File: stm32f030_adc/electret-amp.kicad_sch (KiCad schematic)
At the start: 11 parts, among them Q1 BC337

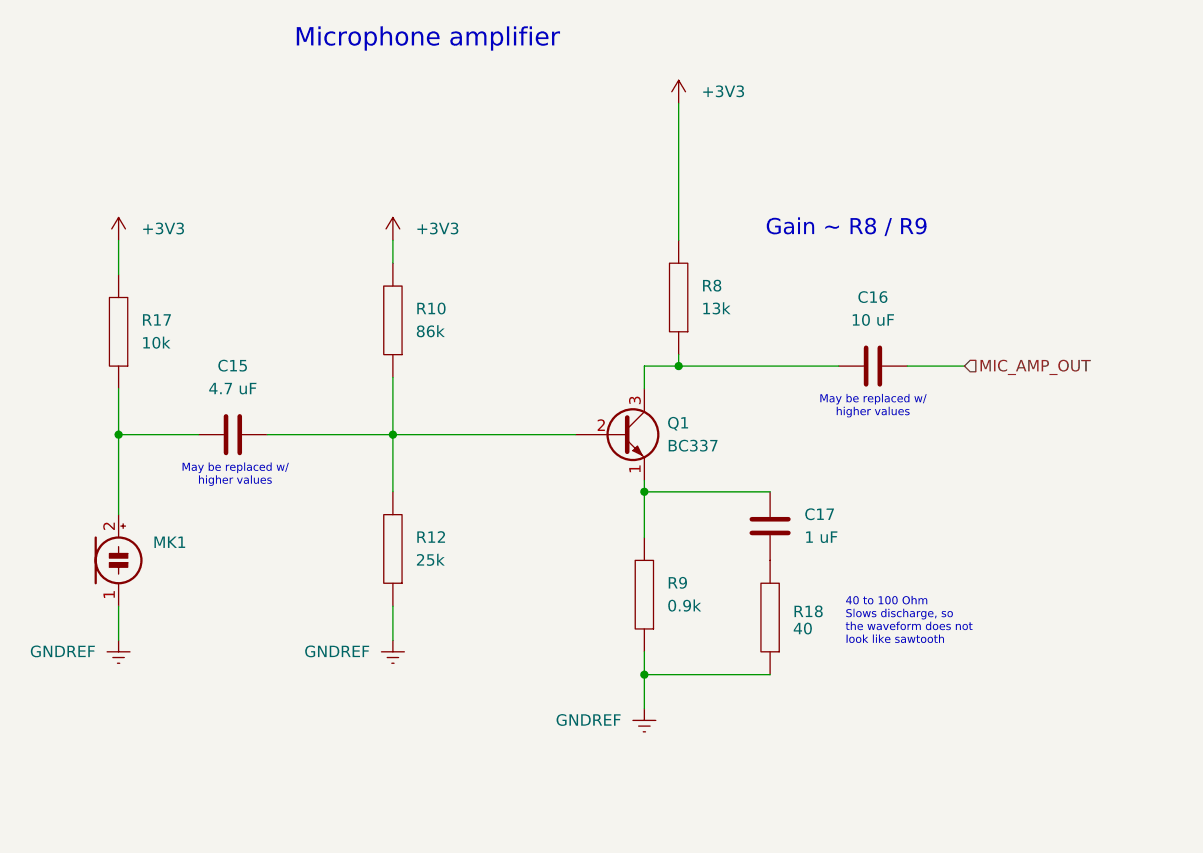
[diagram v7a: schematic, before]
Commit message: [schematics] Impl |  Extensibility: more 0-jumpers
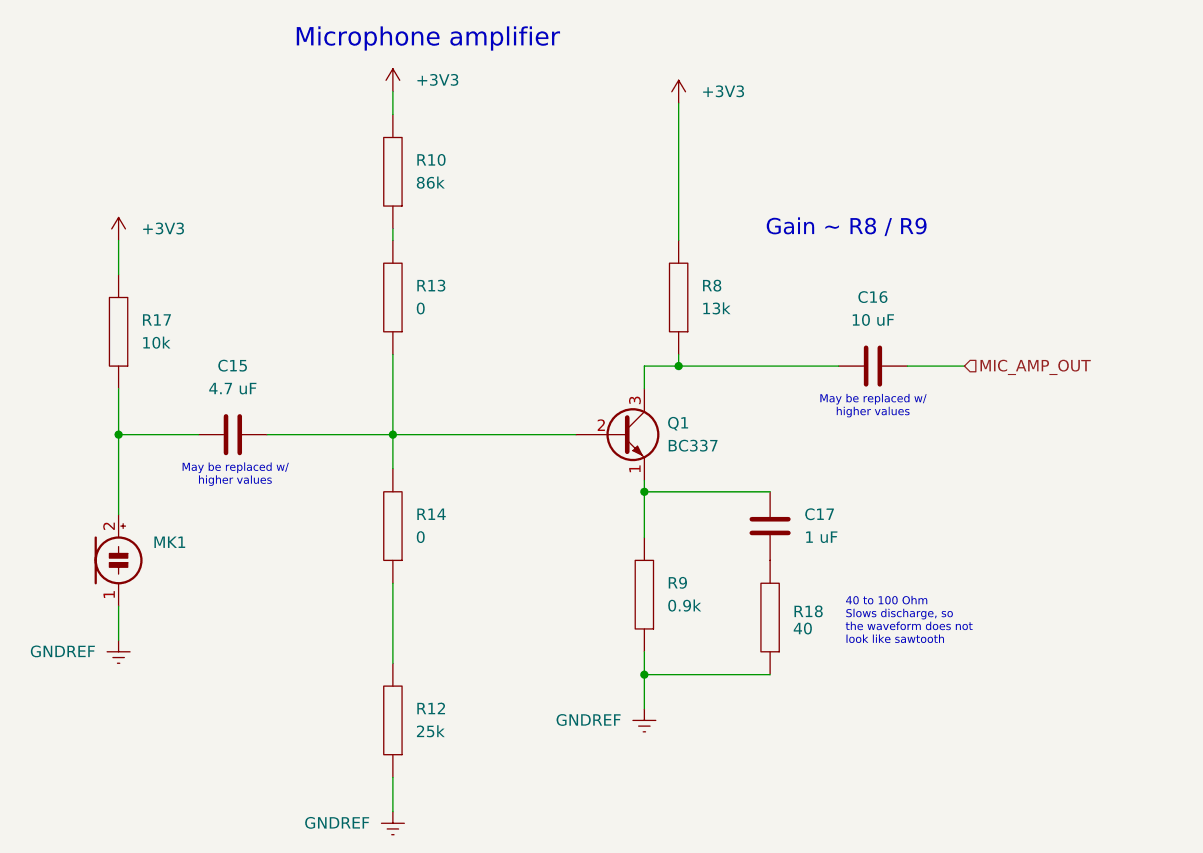
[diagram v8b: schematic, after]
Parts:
- added R13, R14: 0, Resistor_THT:R_Axial_DIN0207_L6.3mm_D2.5mm_P10.16mm_Horizontal, symbol pspice:R
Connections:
- net at C15.2, Q1.2 (B): now also R13.1, R14.2; no longer R10.1, R12.2
- new net: R12.2, R14.1
- new net: R10.1, R13.2
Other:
- moved on the sheet: R10, R12
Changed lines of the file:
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@@
 	(wire
 		(pts
-			(xy 125.73 81.28) (xy 125.73 78.74)
+			(xy 125.73 64.77) (xy 125.73 62.23)
+		)
+		(stroke
+			(width 0)
+			(type default)
+		)
+	)
+	(wire
+		(pts
+			(xy 125.73 91.44) (xy 125.73 100.33)
 		)
 		(stroke
@@
 	(wire
 		(pts
+			(xy 125.73 116.84) (xy 125.73 125.73)
+		)
+		(stroke
+			(width 0)
+			(type default)
+		)
+	)
+	(wire
+		(pts
 			(xy 95.25 100.33) (xy 104.14 100.33)
 		)
@@
 	(wire
 		(pts
-			(xy 125.73 93.98) (xy 125.73 100.33)
+			(xy 125.73 77.47) (xy 125.73 78.74)
 		)
 		(stroke
@@
 	(wire
 		(pts
-			(xy 125.73 100.33) (xy 125.73 106.68)
-		)
-		(stroke
-			(width 0)
-			(type default)
-		)
-	)
-	(wire
-		(pts
-			(xy 125.73 119.38) (xy 125.73 123.19)
+			(xy 125.73 100.33) (xy 125.73 104.14)
+		)
+		(stroke
+			(width 0)
+			(type default)
+		)
+	)
+	(wire
+		(pts
+			(xy 125.73 138.43) (xy 125.73 142.24)
 		)
 		(stroke
@@
 	(symbol
 		(lib_id "power:+3V3")
-		(at 125.73 78.74 0)
+		(at 125.73 62.23 0)
 		(unit 1)
 		(exclude_from_sim no)
@@
 		(fields_autoplaced yes)
 		(property "Reference" "#PWR011"
-			(at 125.73 82.55 0)
+			(at 125.73 66.04 0)
 			(effects
 				(font
@@
 		)
 		(property "Value" "+3V3"
-			(at 128.27 77.4699 0)
+			(at 128.27 60.9599 0)
 			(effects
 				(font
@@
 		)
 		(property "Footprint" ""
-			(at 125.73 78.74 0)
+			(at 125.73 62.23 0)
 			(effects
 				(font
@@
 		)
 		(property "Datasheet" ""
-			(at 125.73 78.74 0)
-			(effects
-				(font
-					(size 1.27 1.27)
-				)
-				(hide yes)
-			)
-		)
-		(property "Description" ""
-			(at 125.73 78.74 0)
+			(at 125.73 62.23 0)
+			(effects
+				(font
+					(size 1.27 1.27)
+				)
+				(hide yes)
+			)
+		)
+		(property "Description" ""
+			(at 125.73 62.23 0)
 			(effects
 				(font
@@
 	)
 	(symbol
+		(lib_id "pspice:R")
+		(at 125.73 110.49 180)
+		(unit 1)
+		(exclude_from_sim no)
+		(in_bom yes)
+		(on_board yes)
+		(dnp no)
+		(fields_autoplaced yes)
+		(property "Reference" "R14"
+			(at 128.27 109.2199 0)
+			(effects
+				(font
+					(size 1.27 1.27)
+				)
+				(justify right)
+			)
+		)
+		(property "Value" "0"
+			(at 128.27 111.7599 0)
+			(effects
+				(font
+					(size 1.27 1.27)
+				)
+				(justify right)
+			)
+		)
+		(property "Footprint" "Resistor_THT:R_Axial_DIN0207_L6.3mm_D2.5mm_P10.16mm_Horizontal"
+			(at 125.73 110.49 0)
+			(effects
+				(font
+					(size 1.27 1.27)
+				)
+				(hide yes)
+			)
+		)
+		(property "Datasheet" "~"
+			(at 125.73 110.49 0)
+			(effects
+				(font
+					(size 1.27 1.27)
+				)
+				(hide yes)
+			)
+		)
+		(property "Description" ""
+			(at 125.73 110.49 0)
+			(effects
+				(font
+					(size 1.27 1.27)
+				)
+				(hide yes)
+			)
+		)
+		(pin "1"
+		)
+		(pin "2"
+		)
+		(instances
+			(project "stm32f030_adc"
+				(path "/85629656-c73b-4e1f-b8e8-4366f4b01266/f519304b-9da7-41e0-88ca-532cf10653e0"
+					(reference "R14")
+					(unit 1)
+				)
+			)
+		)
+	)
+	(symbol
 		(lib_id "Transistor_BJT:2N3904")
 		(at 151.13 100.33 0)
@@
 	(symbol
 		(lib_id "pspice:R")
+		(at 125.73 85.09 180)
+		(unit 1)
+		(exclude_from_sim no)
+		(in_bom yes)
+		(on_board yes)
+		(dnp no)
+		(fields_autoplaced yes)
+		(property "Reference" "R13"
+			(at 128.27 83.8199 0)
+			(effects
+				(font
+					(size 1.27 1.27)
+				)
+				(justify right)
+			)
+		)
+		(property "Value" "0"
+			(at 128.27 86.3599 0)
+			(effects
+				(font
+					(size 1.27 1.27)
+				)
+				(justify right)
+			)
+		)
+		(property "Footprint" "Resistor_THT:R_Axial_DIN0207_L6.3mm_D2.5mm_P10.16mm_Horizontal"
+			(at 125.73 85.09 0)
+			(effects
+				(font
+					(size 1.27 1.27)
+				)
+				(hide yes)
+			)
+		)
+		(property "Datasheet" "~"
+			(at 125.73 85.09 0)
+			(effects
+				(font
+					(size 1.27 1.27)
+				)
+				(hide yes)
+			)
+		)
+		(property "Description" ""
+			(at 125.73 85.09 0)
+			(effects
+				(font
+					(size 1.27 1.27)
+				)
+				(hide yes)
+			)
+		)
+		(pin "1"
+		)
+		(pin "2"
+		)
+		(instances
+			(project "stm32f030_adc"
+				(path "/85629656-c73b-4e1f-b8e8-4366f4b01266/f519304b-9da7-41e0-88ca-532cf10653e0"
+					(reference "R13")
+					(unit 1)
+				)
+			)
+		)
+	)
+	(symbol
+		(lib_id "pspice:R")
 		(at 153.67 118.11 180)
 		(unit 1)
@@
 	(symbol
 		(lib_id "pspice:R")
-		(at 125.73 113.03 180)
+		(at 125.73 132.08 180)
 		(unit 1)
 		(exclude_from_sim no)
@@
 		(fields_autoplaced yes)
 		(property "Reference" "R12"
-			(at 128.27 111.7599 0)
+			(at 128.27 130.8099 0)
 			(effects
 				(font
@@
 		)
 		(property "Value" "25k"
-			(at 128.27 114.2999 0)
+			(at 128.27 133.3499 0)
 			(effects
 				(font
@@
 		)
 		(property "Footprint" "Resistor_THT:R_Axial_DIN0207_L6.3mm_D2.5mm_P10.16mm_Horizontal"
-			(at 125.73 113.03 0)
+			(at 125.73 132.08 0)
 			(effects
 				(font
@@
 		)
 		(property "Datasheet" "~"
-			(at 125.73 113.03 0)
-			(effects
-				(font
-					(size 1.27 1.27)
-				)
-				(hide yes)
-			)
-		)
-		(property "Description" ""
-			(at 125.73 113.03 0)
+			(at 125.73 132.08 0)
+			(effects
+				(font
+					(size 1.27 1.27)
+				)
+				(hide yes)
+			)
+		)
+		(property "Description" ""
+			(at 125.73 132.08 0)
 			(effects
 				(font
@@
 	(symbol
 		(lib_id "pspice:R")
-		(at 125.73 87.63 180)
+		(at 125.73 71.12 180)
 		(unit 1)
 		(exclude_from_sim no)
@@
 		(fields_autoplaced yes)
 		(property "Reference" "R10"
-			(at 128.27 86.3599 0)
+			(at 128.27 69.8499 0)
 			(effects
 				(font
@@
 		)
 		(property "Value" "86k"
-			(at 128.27 88.8999 0)
+			(at 128.27 72.3899 0)
 			(effects
 				(font
@@
 		)
 		(property "Footprint" "Resistor_THT:R_Axial_DIN0207_L6.3mm_D2.5mm_P10.16mm_Horizontal"
-			(at 125.73 87.63 0)
+			(at 125.73 71.12 0)
 			(effects
 				(font
@@
 		)
 		(property "Datasheet" "~"
-			(at 125.73 87.63 0)
-			(effects
-				(font
-					(size 1.27 1.27)
-				)
-				(hide yes)
-			)
-		)
-		(property "Description" ""
-			(at 125.73 87.63 0)
+			(at 125.73 71.12 0)
+			(effects
+				(font
+					(size 1.27 1.27)
+				)
+				(hide yes)
+			)
+		)
+		(property "Description" ""
+			(at 125.73 71.12 0)
 			(effects
 				(font
@@
 	(symbol
 		(lib_id "power:GNDREF")
-		(at 125.73 123.19 0)
+		(at 125.73 142.24 0)
 		(mirror y)
 		(unit 1)
@@
 		(fields_autoplaced yes)
 		(property "Reference" "#PWR012"
-			(at 125.73 129.54 0)
+			(at 125.73 148.59 0)
 			(effects
 				(font
@@
 		)
 		(property "Value" "GNDREF"
-			(at 123.19 124.4599 0)
+			(at 123.19 143.5099 0)
 			(effects
 				(font
@@
 		)
 		(property "Footprint" ""
-			(at 125.73 123.19 0)
+			(at 125.73 142.24 0)
 			(effects
 				(font
@@
 		)
 		(property "Datasheet" ""
-			(at 125.73 123.19 0)
-			(effects
-				(font
-					(size 1.27 1.27)
-				)
-				(hide yes)
-			)
-		)
-		(property "Description" ""
-			(at 125.73 123.19 0)
-			(effects
-				(font
+			(at 125.73 142.24 0)
+			(effects
+				(font
+					(size 1.27 1.27)
+				)
+				(hide yes)
+			)
+		)
+		(property "Description" ""
+			(at 125.73 142.24 0)
+			(effects
+				(font
